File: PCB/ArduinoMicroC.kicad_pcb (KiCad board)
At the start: 4 copper layers, 18 x 36.2 mm, 28 parts, among them J1 USB_C_Receptacle_USB2.0, J2 Conn_01x12, J3 Conn_01x06, J4 Conn_01x12, SW1 SW_Check_USB, SW2 SW_Push, U1 MIC5219-5.0YM5, U2 ATmega32U4-MU, Y1 16MHz

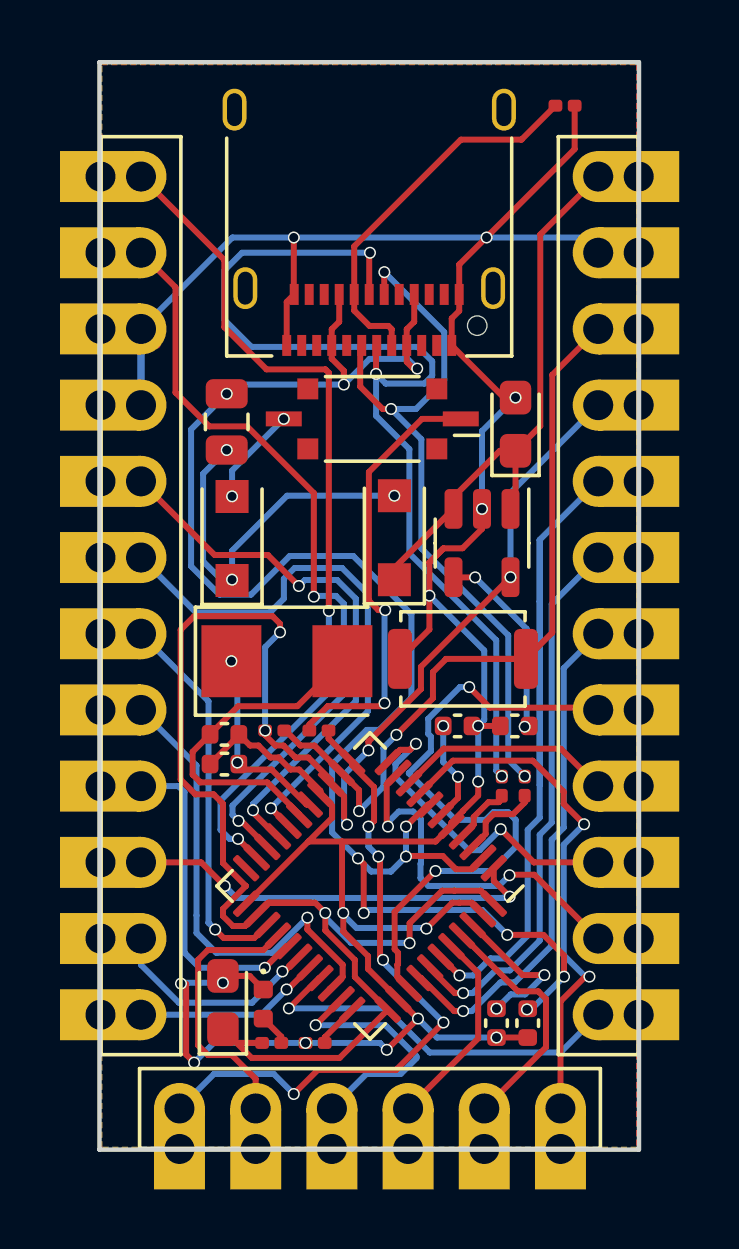
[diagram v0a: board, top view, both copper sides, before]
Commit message: Add label into headers
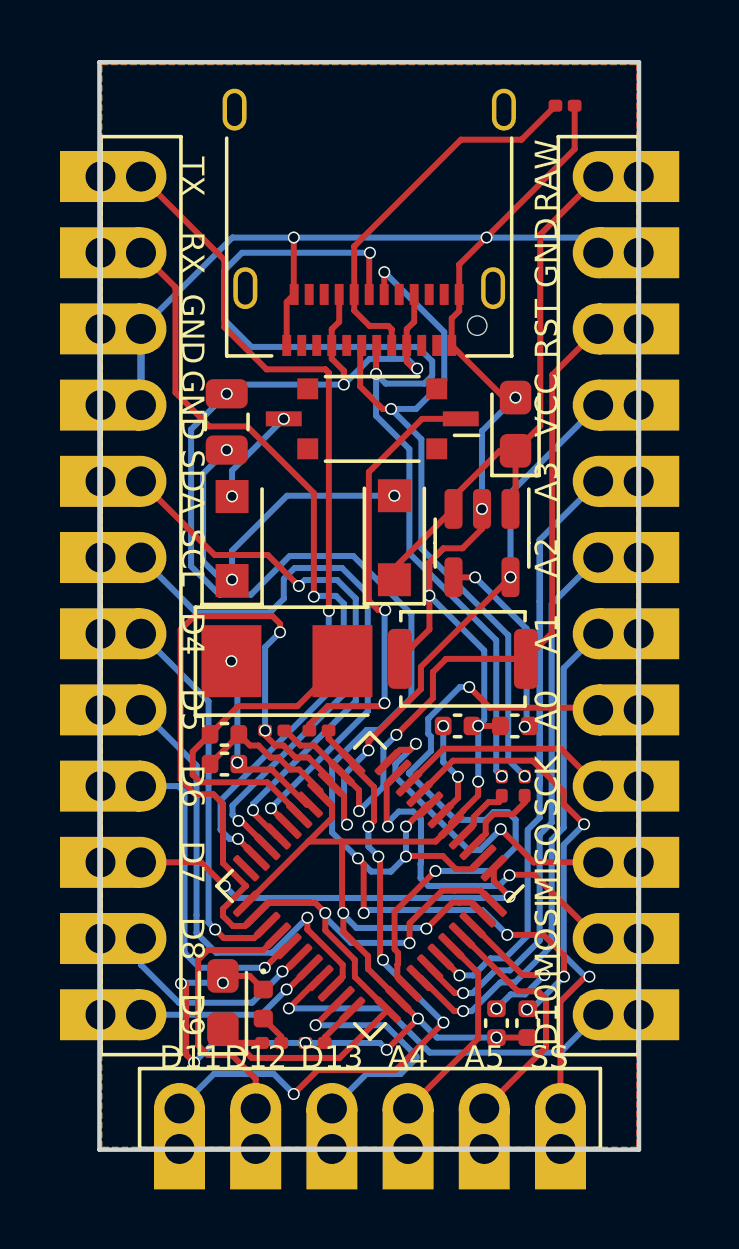
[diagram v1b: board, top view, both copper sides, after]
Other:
- board text added: "A0"
- board text added: "A1"
- board text added: "A2"
- board text added: "A3"
- board text added: "A4"
- board text added: "A5"
- board text added: "D10"
- board text added: "D11"
- board text added: "D12"
- board text added: "D13"
- board text added: "D4"
- board text added: "D5"
- board text added: "D6"
- board text added: "D7"
- board text added: "D8"
- board text added: "D9"
- board text added: "GND"
- board text added: "MISO"
- board text added: "MOSI"
- board text added: "RAW"
- board text added: "RST"
- board text added: "RX"
- board text added: "SCK"
- board text added: "SCL"
- board text added: "SDA"
- board text added: "SS"
- board text added: "TX"
- board text added: "VCC"

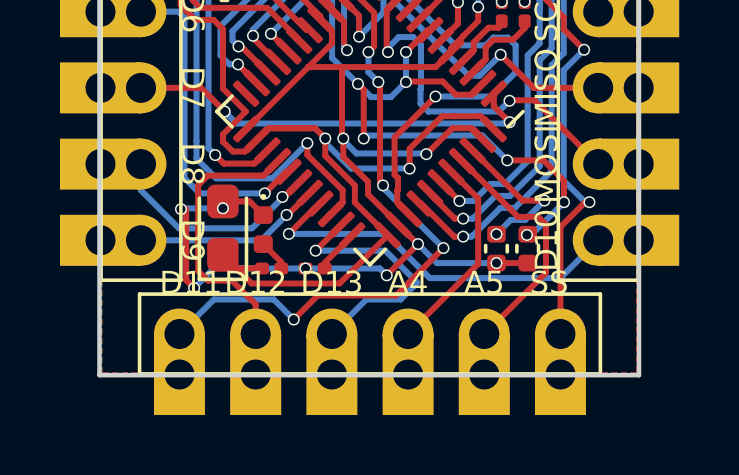
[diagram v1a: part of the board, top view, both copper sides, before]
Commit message: Update SilkS layer
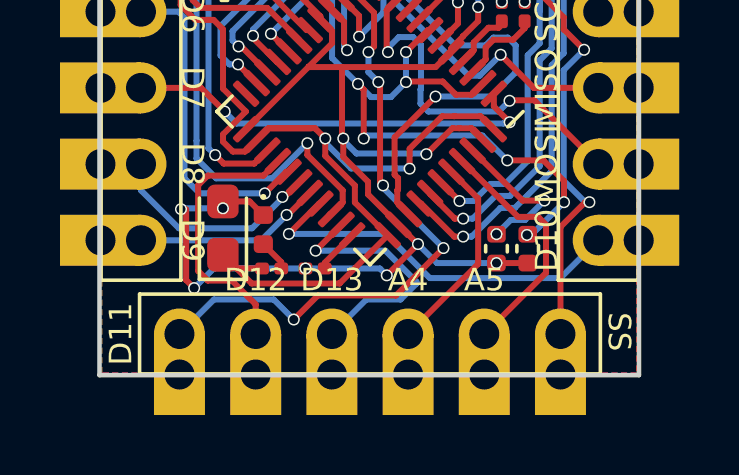
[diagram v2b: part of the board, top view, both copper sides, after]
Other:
- board text added: "Neih-Tech Arduino Micro-C"
